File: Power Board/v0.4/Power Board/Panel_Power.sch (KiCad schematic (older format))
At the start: 19 parts, among them U2 TPS53819A, U3 CSD86360Q5D

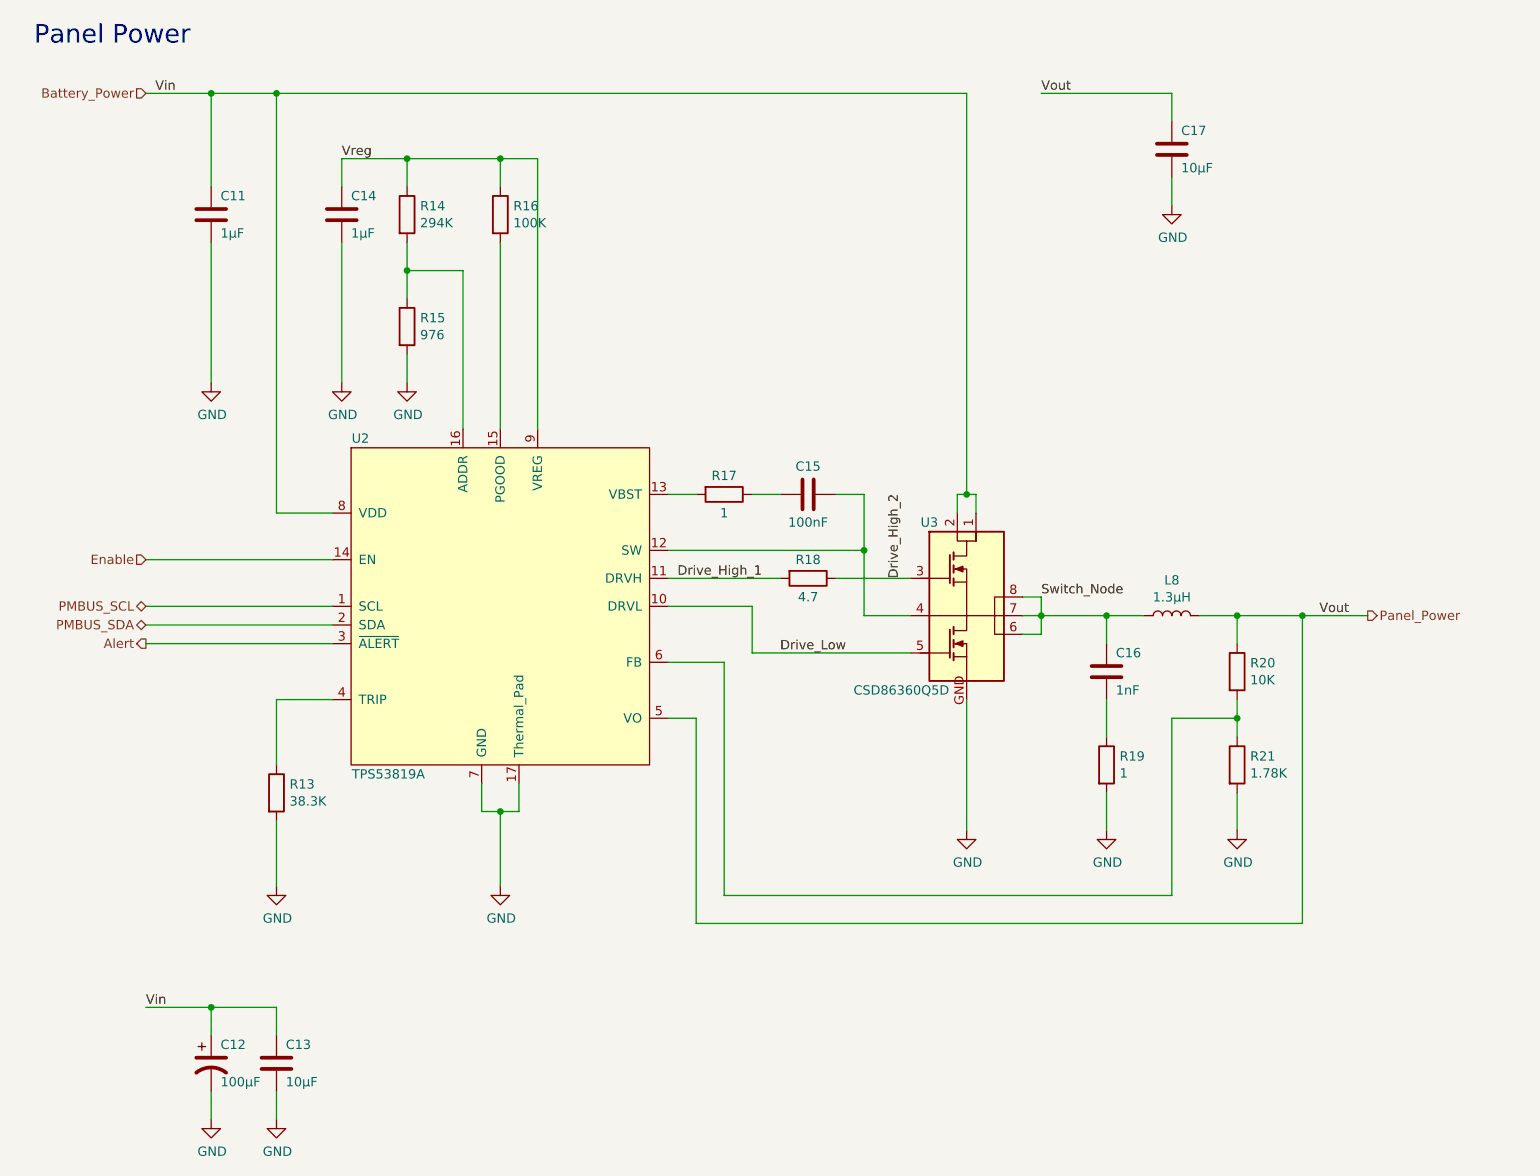
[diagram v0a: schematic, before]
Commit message: Update panel power with Cin, Cout.
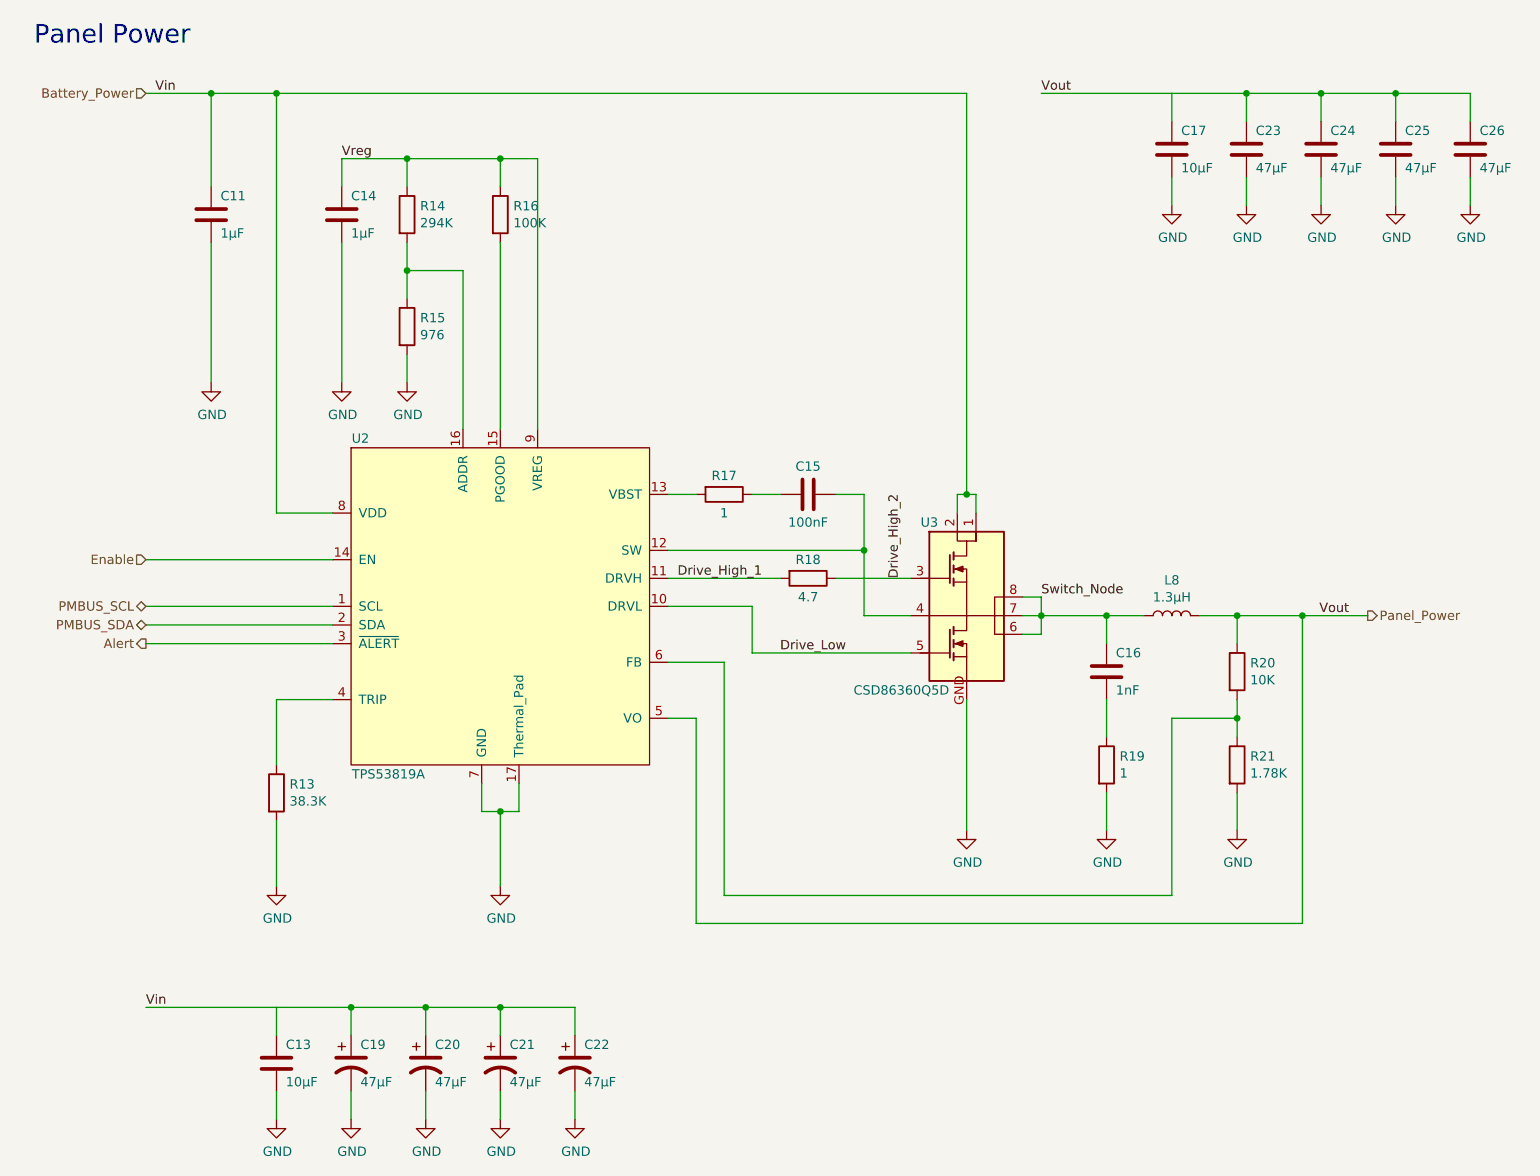
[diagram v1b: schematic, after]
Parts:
- removed C12: 100µF, Capacitor_SMD:CP_Elec_8x10, symbol Device:CP1
- added C19, C20, C21, C22: 47µF, Power_Board:CP_OSCON_Poly_F12, symbol Device:CP1
- added C23, C24, C25, C26: 47µF, Capacitor_SMD:C_1210_3225Metric, symbol Device:C
- C13, C17: footprint Capacitor_SMD:C_0805_2012Metric -> Capacitor_SMD:C_1206_3216Metric
- C14: footprint Capacitor_SMD:C_0805_2012Metric -> Capacitor_SMD:C_0603_1608Metric
- R13: footprint Resistor_SMD:R_0805_2012Metric -> Resistor_SMD:R_0603_1608Metric; Digikey No. 541-38.3KCCT-ND -> (none); Manufacturer Vishay-Dale -> (none); Part No. CRCW080538K3FKEA -> (none)
- R21: footprint Resistor_SMD:R_0805_2012Metric -> Resistor_SMD:R_0603_1608Metric; Digikey No. P1.78KCCT-ND -> (none); Manufacturer Panasonic -> (none); Part No. ERJ-6ENF1781V -> (none)
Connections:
- net Battery_Power: now also C19.1, C20.1, C21.1, C22.1
- net GND: now also C19.2, C20.2, C21.2, C22.2, C23.2, C24.2, C25.2, C26.2
- net Panel_Power: now also C23.1, C24.1, C25.1, C26.1

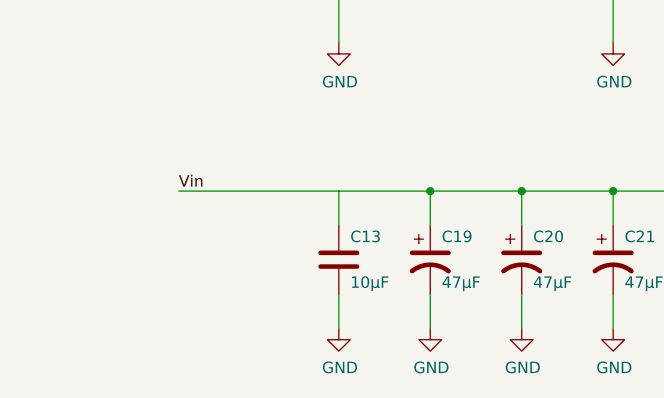
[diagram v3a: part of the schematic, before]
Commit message: Final Cleanup 2 DRC Errors that seem false Silkscreen needs work
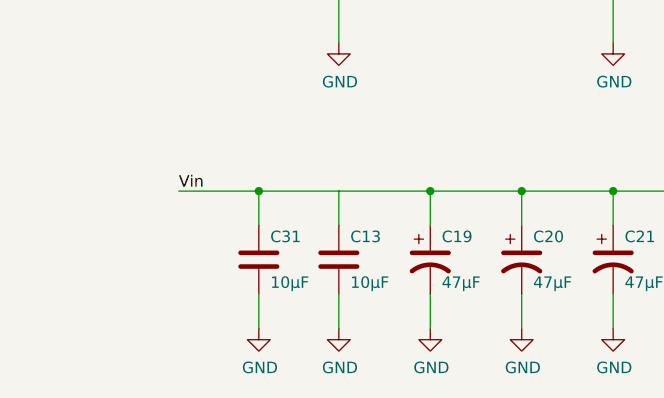
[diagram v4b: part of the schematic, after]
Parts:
- added C31: 10µF, Capacitor_SMD:C_1206_3216Metric, symbol Device:C
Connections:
- net Battery_Power: now also C31.1
- net GND: now also C31.2
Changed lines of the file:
@@
 	8900 1600 9300 1600
 Wire Wire Line
-	2200 6500 2900 6500
+	2200 6500 2550 6500
+$Comp
+L Device:C C31
+U 1 1 5CD68772
+P 2550 6800
+F 0 "C31" H 2600 6900 50  0000 L CNN
+F 1 "10µF" H 2600 6700 50  0000 L CNN
+F 2 "Capacitor_SMD:C_1206_3216Metric" H 2588 6650 50  0001 C CNN
+F 3 "~" H 2550 6800 50  0001 C CNN
+F 4 "490-10748-1-ND" H -350 0   50  0001 C CNN "Digikey No."
+F 5 "Murata" H -350 0   50  0001 C CNN "Manufacturer"
+F 6 " GRM21BR61E106MA73L " H -350 0   50  0001 C CNN "Part No."
+	1    2550 6800
+	1    0    0    -1
+$EndComp
+$Comp
+L power:GND #PWR?
+U 1 1 5CD694DC
+P 2550 7100
+F 0 "#PWR?" H 2550 6850 50  0001 C CNN
+F 1 "GND" H 2555 6927 50  0000 C CNN
+F 2 "" H 2550 7100 50  0001 C CNN
+F 3 "" H 2550 7100 50  0001 C CNN
+	1    2550 7100
+	1    0    0    -1
+$EndComp
+Wire Wire Line
+	2550 6650 2550 6500
+Connection ~ 2550 6500
+Wire Wire Line
+	2550 6500 2900 6500
+Wire Wire Line
+	2550 6950 2550 7100
 $EndSCHEMATC

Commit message: Add 3D models for more components.
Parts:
- U2: footprint Package_DFN_QFN:VQFN-16-1EP_3x3mm_P0.5mm_EP1.68x1.68mm_ThermalVias -> Power_Board:VQFN-16-1EP_3x3mm_P0.5mm_EP1.68x1.68mm_ThermalVias
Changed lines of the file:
@@
 F 0 "U2" H 3350 5250 50  0000 C CNN
 F 1 "TPS53819A" H 3500 3450 50  0000 C CNN
-F 2 "Package_DFN_QFN:VQFN-16-1EP_3x3mm_P0.5mm_EP1.68x1.68mm_ThermalVias" H 4100 4350 50  0001 C CNN
+F 2 "Power_Board:VQFN-16-1EP_3x3mm_P0.5mm_EP1.68x1.68mm_ThermalVias" H 4100 4350 50  0001 C CNN
 F 3 "" H 4100 4350 50  0001 C CNN
 F 4 "TPS53819ARGTR" H -100 0   50  0001 C CNN "Part No."

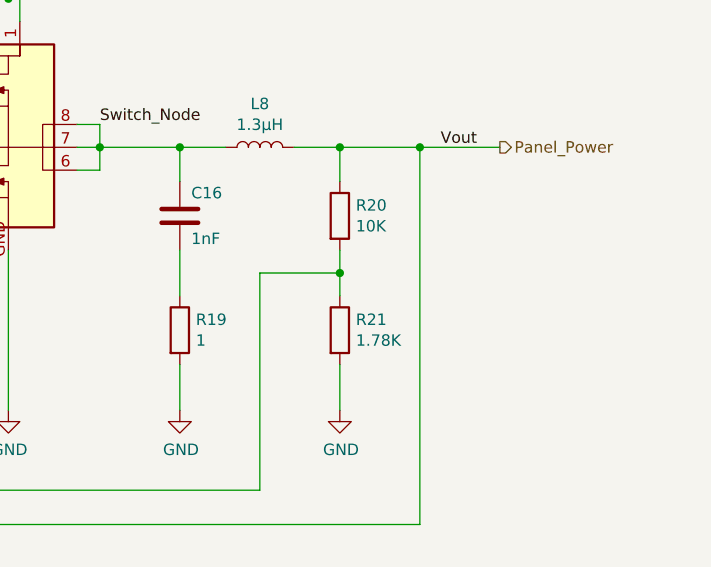
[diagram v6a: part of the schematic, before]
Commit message: Update BOM.  Change R20 to 0603 package.
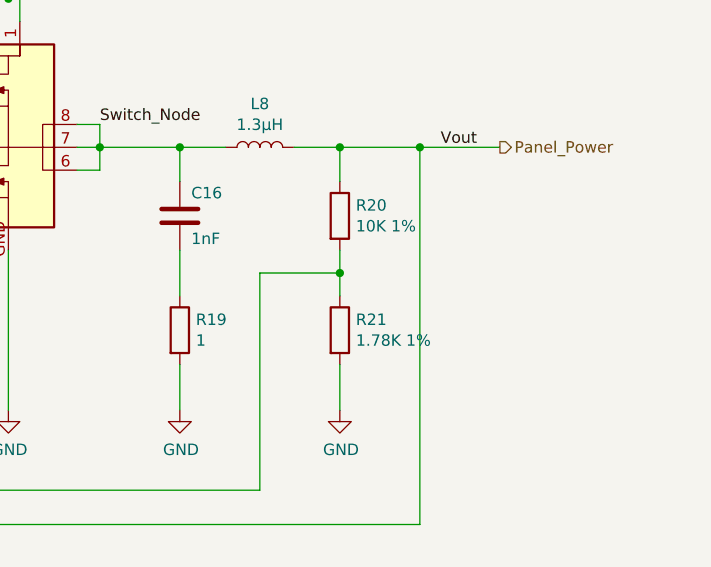
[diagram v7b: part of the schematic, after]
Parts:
- C13, C17, C31: Part No. GRM21BR61E106MA73L -> GRM21BR61E106MA73L
- C19, C20, C21, C22: Part No. 35SVPD47M -> 35SVPD47M
- C23, C24, C25, C26: Part No. GRM32EC81C476KE15L -> GRM32EC81C476KE15L
- R13: Digikey No. (none) -> RMCF0603FT38K3CT-ND; Manufacturer (none) -> Stackpole; Part No. (none) -> RMCF0603FT38K3
- R20: value 10K -> 10K 1%; footprint Resistor_SMD:R_0402_1005Metric -> Resistor_SMD:R_0603_1608Metric; Digikey No. RMCF0402FT10K0CT-ND -> RNCP0603FTD10K0CT-ND; Part No. RMCF0402FT10K0 -> RNCP0603FTD10K0
- R21: value 1.78K -> 1.78K 1%; Digikey No. (none) -> 311-17.8KHRCT-ND; Manufacturer (none) -> Yageo; Part No. (none) -> RC0603FR-0717K8L
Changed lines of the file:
@@
 F 2 "Resistor_SMD:R_0603_1608Metric" V 2830 5350 50  0001 C CNN
 F 3 "~" H 2900 5350 50  0001 C CNN
+F 4 "RMCF0603FT38K3CT-ND" H 0   0   50  0001 C CNN "Digikey No."
+F 5 "Stackpole" H 0   0   50  0001 C CNN "Manufacturer"
+F 6 "RMCF0603FT38K3" H 0   0   50  0001 C CNN "Part No."
 	1    2900 5350
 	1    0    0    -1
@@
 F 4 "490-10748-1-ND" H -450 0   50  0001 C CNN "Digikey No."
 F 5 "Murata" H -450 0   50  0001 C CNN "Manufacturer"
-F 6 " GRM21BR61E106MA73L " H -450 0   50  0001 C CNN "Part No."
+F 6 "GRM21BR61E106MA73L" H -450 0   50  0001 C CNN "Part No."
 	1    7700 1900
 	1    0    0    -1
@@
 P 8050 5200
 F 0 "R21" H 8120 5246 50  0000 L CNN
-F 1 "1.78K" H 8120 5155 50  0000 L CNN
+F 1 "1.78K 1%" H 8120 5155 50  0000 L CNN
 F 2 "Resistor_SMD:R_0603_1608Metric" V 7980 5200 50  0001 C CNN
 F 3 "~" H 8050 5200 50  0001 C CNN
+F 4 "311-17.8KHRCT-ND" H 0   0   50  0001 C CNN "Digikey No."
+F 5 "Yageo" H 0   0   50  0001 C CNN "Manufacturer"
+F 6 "RC0603FR-0717K8L" H 0   0   50  0001 C CNN "Part No."
 	1    8050 5200
 	1    0    0    -1
@@
 P 8050 4700
 F 0 "R20" H 8120 4746 50  0000 L CNN
-F 1 "10K" H 8120 4655 50  0000 L CNN
-F 2 "Resistor_SMD:R_0402_1005Metric" V 7980 4700 50  0001 C CNN
+F 1 "10K 1%" H 8120 4655 50  0000 L CNN
+F 2 "Resistor_SMD:R_0603_1608Metric" V 7980 4700 50  0001 C CNN
 F 3 "~" H 8050 4700 50  0001 C CNN
-F 4 "RMCF0402FT10K0CT-ND" H 0   0   50  0001 C CNN "Digikey No."
+F 4 "RNCP0603FTD10K0CT-ND" H 0   0   50  0001 C CNN "Digikey No."
 F 5 "Stackpole" H 0   0   50  0001 C CNN "Manufacturer"
-F 6 "RMCF0402FT10K0" H 0   0   50  0001 C CNN "Part No."
+F 6 "RNCP0603FTD10K0" H 0   0   50  0001 C CNN "Part No."
 	1    8050 4700
 	1    0    0    -1
@@
 F 4 "490-10748-1-ND" H 0   0   50  0001 C CNN "Digikey No."
 F 5 "Murata" H 0   0   50  0001 C CNN "Manufacturer"
-F 6 " GRM21BR61E106MA73L " H 0   0   50  0001 C CNN "Part No."
+F 6 "GRM21BR61E106MA73L" H 0   0   50  0001 C CNN "Part No."
 	1    2900 6800
 	1    0    0    -1
@@
 F 4 "PCE5080CT-ND" H 0   0   50  0001 C CNN "Digikey No."
 F 5 "Panasonic" H 0   0   50  0001 C CNN "Manufacturer"
-F 6 " 35SVPD47M " H 0   0   50  0001 C CNN "Part No."
+F 6 "35SVPD47M" H 0   0   50  0001 C CNN "Part No."
 	1    3300 6800
 	1    0    0    -1
@@
 F 4 "PCE5080CT-ND" H 0   0   50  0001 C CNN "Digikey No."
 F 5 "Panasonic" H 0   0   50  0001 C CNN "Manufacturer"
-F 6 " 35SVPD47M " H 0   0   50  0001 C CNN "Part No."
+F 6 "35SVPD47M" H 0   0   50  0001 C CNN "Part No."
 	1    3700 6800
 	1    0    0    -1
@@
 F 4 "PCE5080CT-ND" H 0   0   50  0001 C CNN "Digikey No."
 F 5 "Panasonic" H 0   0   50  0001 C CNN "Manufacturer"
-F 6 " 35SVPD47M " H 0   0   50  0001 C CNN "Part No."
+F 6 "35SVPD47M" H 0   0   50  0001 C CNN "Part No."
 	1    4100 6800
 	1    0    0    -1
@@
 F 4 "PCE5080CT-ND" H 0   0   50  0001 C CNN "Digikey No."
 F 5 "Panasonic" H 0   0   50  0001 C CNN "Manufacturer"
-F 6 " 35SVPD47M " H 0   0   50  0001 C CNN "Part No."
+F 6 "35SVPD47M" H 0   0   50  0001 C CNN "Part No."
 	1    4500 6800
 	1    0    0    -1
@@
 F 4 "490-10531-1-ND" H 0   0   50  0001 C CNN "Digikey No."
 F 5 "Murata" H 0   0   50  0001 C CNN "Manufacturer"
-F 6 " GRM32EC81C476KE15L " H 0   0   50  0001 C CNN "Part No."
+F 6 "GRM32EC81C476KE15L" H 0   0   50  0001 C CNN "Part No."
 	1    8100 1900
 	1    0    0    -1
@@
 F 4 "490-10531-1-ND" H 0   0   50  0001 C CNN "Digikey No."
 F 5 "Murata" H 0   0   50  0001 C CNN "Manufacturer"
-F 6 " GRM32EC81C476KE15L " H 0   0   50  0001 C CNN "Part No."
+F 6 "GRM32EC81C476KE15L" H 0   0   50  0001 C CNN "Part No."
 	1    8500 1900
 	1    0    0    -1
@@
 F 4 "490-10531-1-ND" H 0   0   50  0001 C CNN "Digikey No."
 F 5 "Murata" H 0   0   50  0001 C CNN "Manufacturer"
-F 6 " GRM32EC81C476KE15L " H 0   0   50  0001 C CNN "Part No."
+F 6 "GRM32EC81C476KE15L" H 0   0   50  0001 C CNN "Part No."
 	1    8900 1900
 	1    0    0    -1
@@
 F 4 "490-10531-1-ND" H 0   0   50  0001 C CNN "Digikey No."
 F 5 "Murata" H 0   0   50  0001 C CNN "Manufacturer"
-F 6 " GRM32EC81C476KE15L " H 0   0   50  0001 C CNN "Part No."
+F 6 "GRM32EC81C476KE15L" H 0   0   50  0001 C CNN "Part No."
 	1    9300 1900
 	1    0    0    -1
@@
 F 4 "490-10748-1-ND" H -350 0   50  0001 C CNN "Digikey No."
 F 5 "Murata" H -350 0   50  0001 C CNN "Manufacturer"
-F 6 " GRM21BR61E106MA73L " H -350 0   50  0001 C CNN "Part No."
+F 6 "GRM21BR61E106MA73L" H -350 0   50  0001 C CNN "Part No."
 	1    2550 6800
 	1    0    0    -1
